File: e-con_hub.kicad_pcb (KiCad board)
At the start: 2 copper layers, 55 x 25 mm, 7 parts, among them J7 XG4A-1031

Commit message: パターンを微修正
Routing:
- net Net-(J7-Pin_10): track 25.6 -> 26.8 mm
- net Net-(J7-Pin_8): track 11.0 -> 12.2 mm
- net Net-(J7-Pin_9): track 23.8 -> 24.6 mm
- net GND: track 121.0 -> 120.4 mm, vias 27 -> 29

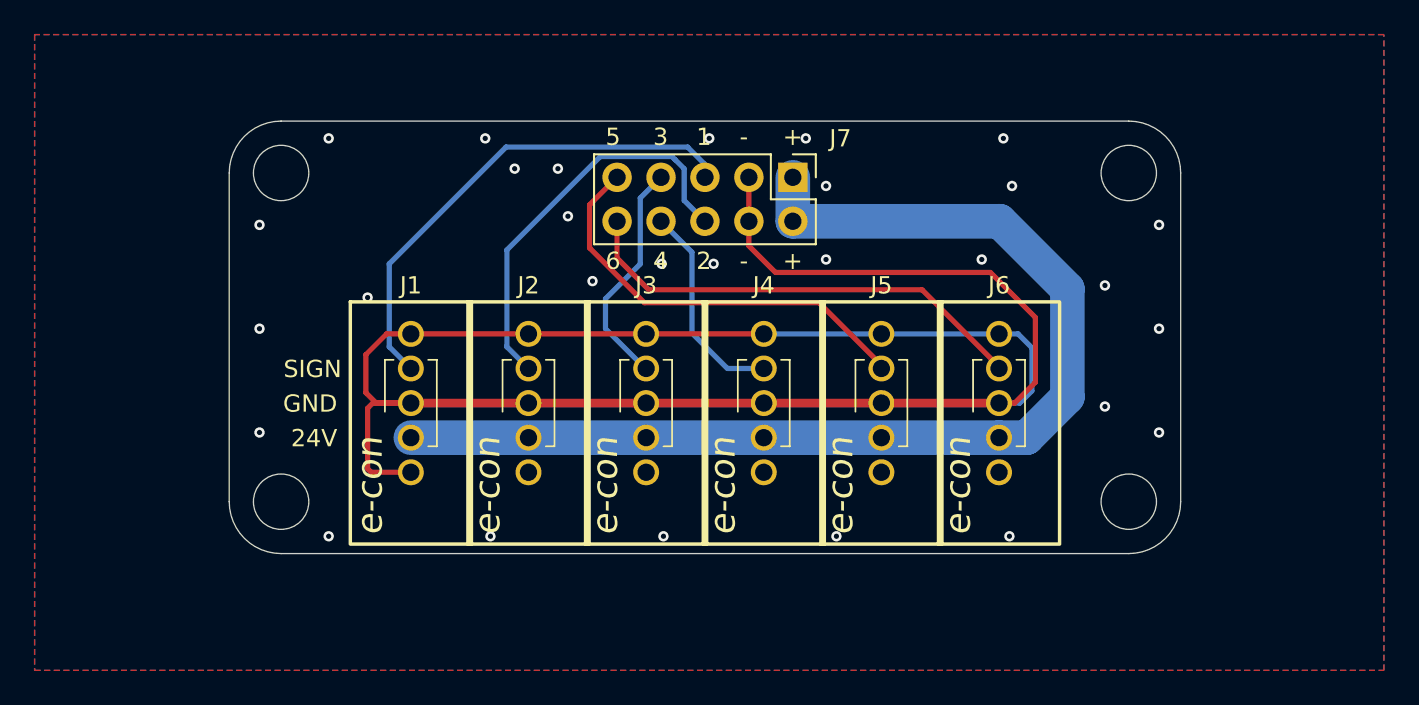
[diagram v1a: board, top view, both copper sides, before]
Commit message: J7をL型milコネクタに変更
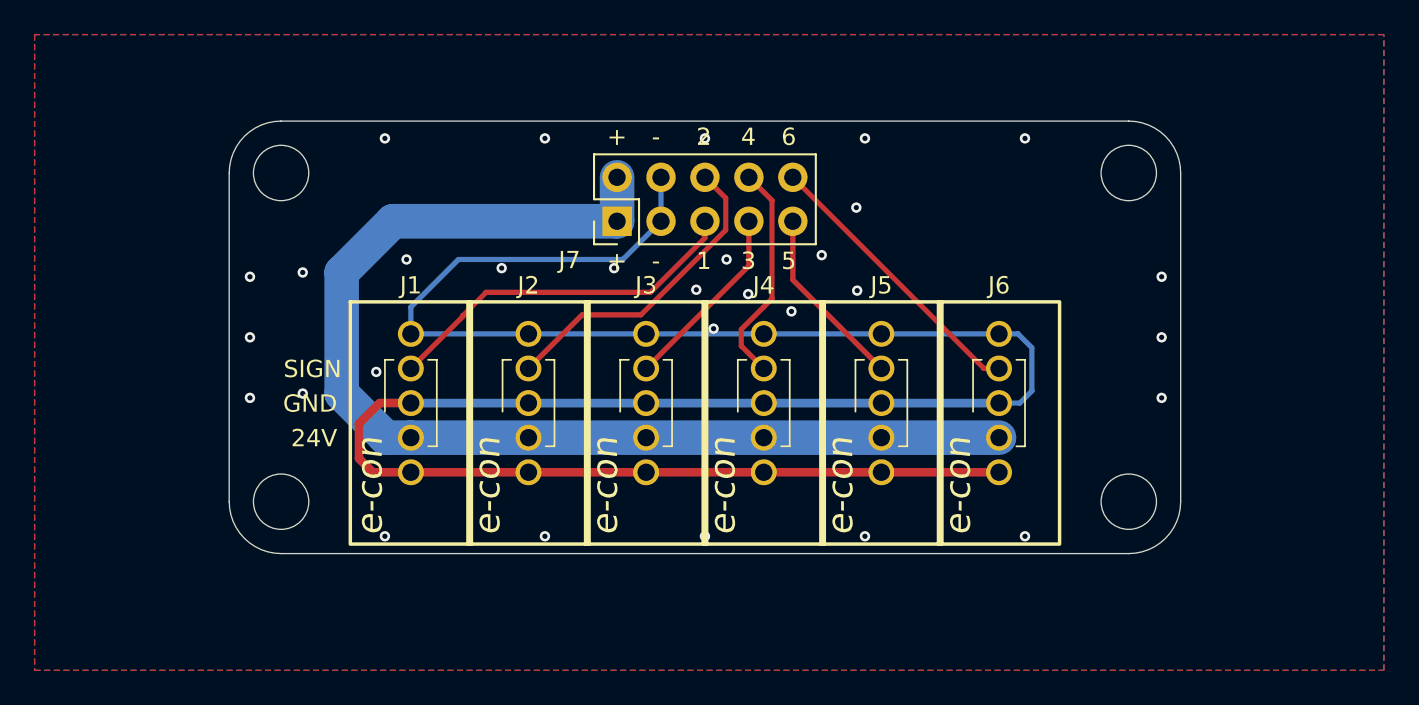
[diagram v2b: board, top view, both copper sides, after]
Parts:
- moved J7 10.5 mm to (149.4, 88.8), turned to 90 degrees
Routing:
- net GND: track 120.4 -> 138.4 mm, vias 29 -> 30
- net Net-(J7-Pin_9): track 24.6 -> 10.6 mm
- net Net-(J7-Pin_10): track 26.8 -> 16.5 mm
- net Net-(J7-Pin_5): track 28.8 -> 21.1 mm
- net Net-(J7-Pin_6): track 23.7 -> 18.3 mm
- net Net-(J7-Pin_7): track 13.4 -> 11.0 mm
- net Net-(J7-Pin_8): track 12.2 -> 12.9 mm
- net +24V: track 65.2 -> 65.7 mm
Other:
- board text added: "e-CON Hub Board Ver1.1 2025/06/06 https://github.com/Akutagawa50/e-con_hub"
- board text removed: "e-CON Hub Board Ver1.0 2025/06/04"
